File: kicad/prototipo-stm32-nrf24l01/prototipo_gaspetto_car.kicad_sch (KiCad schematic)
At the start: 11 parts, among them J1 Conn_01x07_Pin - TEST POINT, M1 Motor_DC, M2 Motor_DC, Q1 BC548, U1 YAAJ_BluePill_Part_Like_SWD_B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, U2 nRF24L01+, U3 L9110-M2, U4 L9110-M1, U5 5 to 3.3v

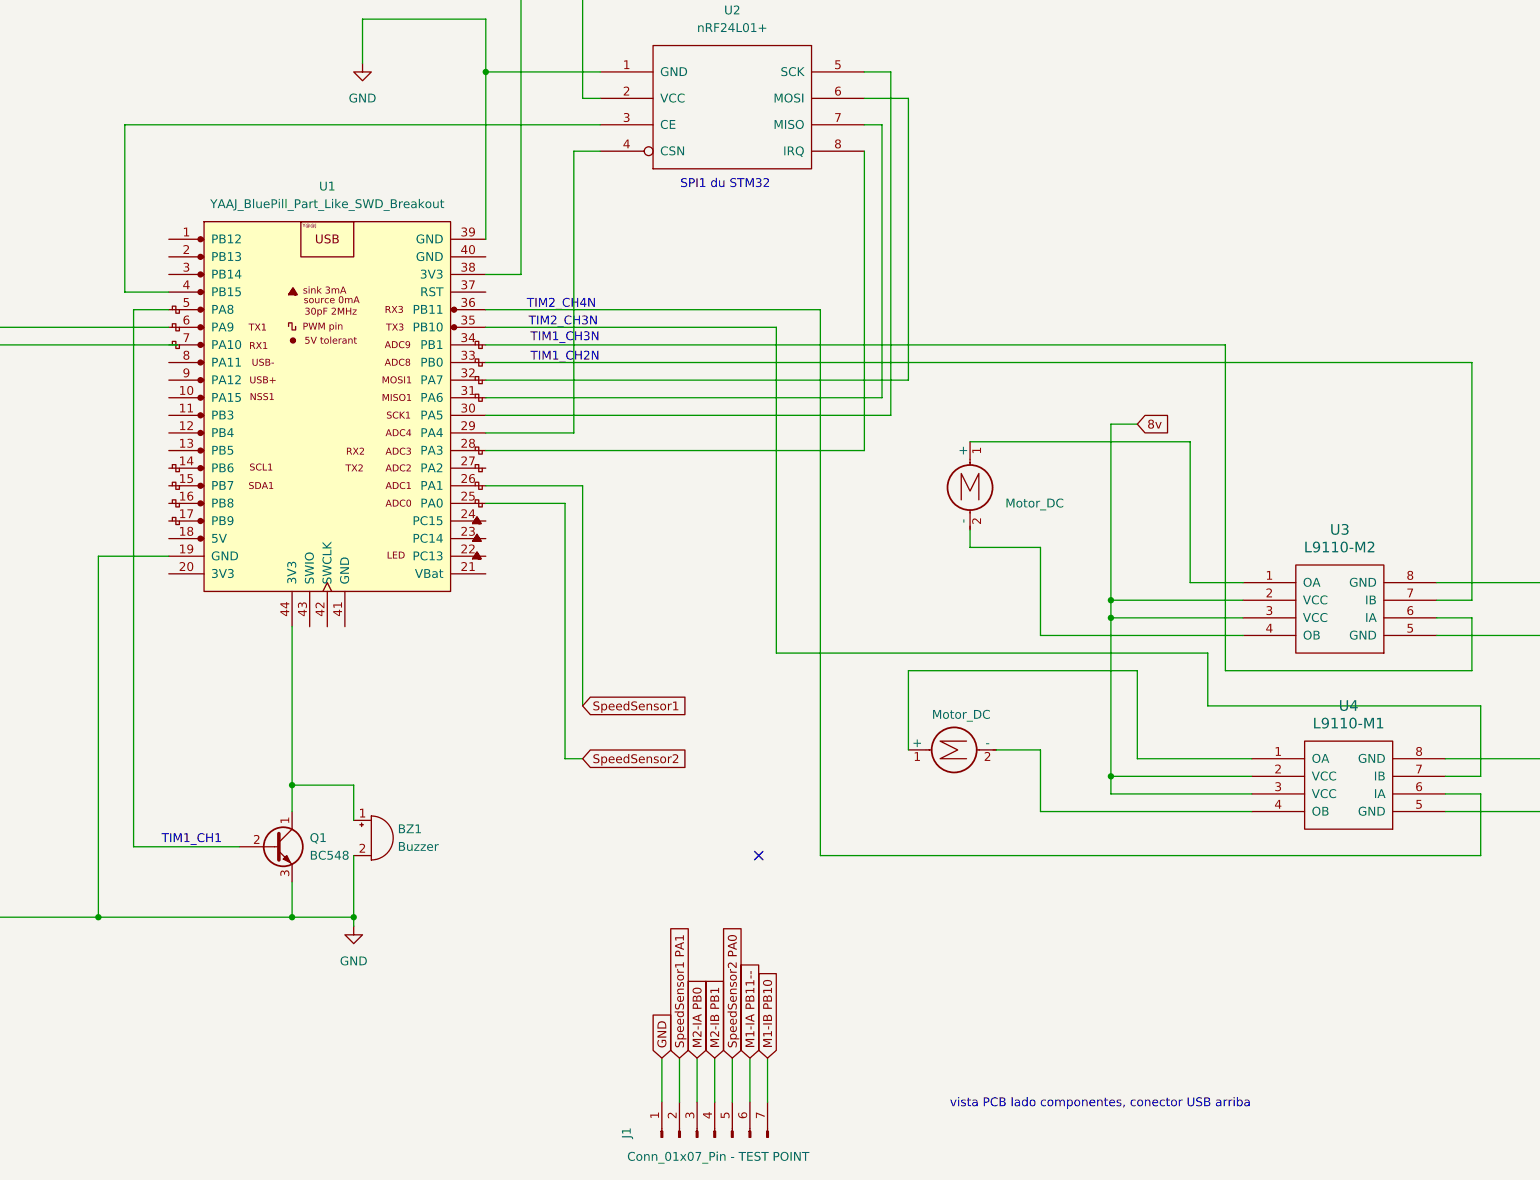
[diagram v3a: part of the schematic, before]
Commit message: car: motor and radio
- We receive radio commands and execute them. I have some issues
  controlling DC motors, will try to restructure a bit and add
  a PID controller.
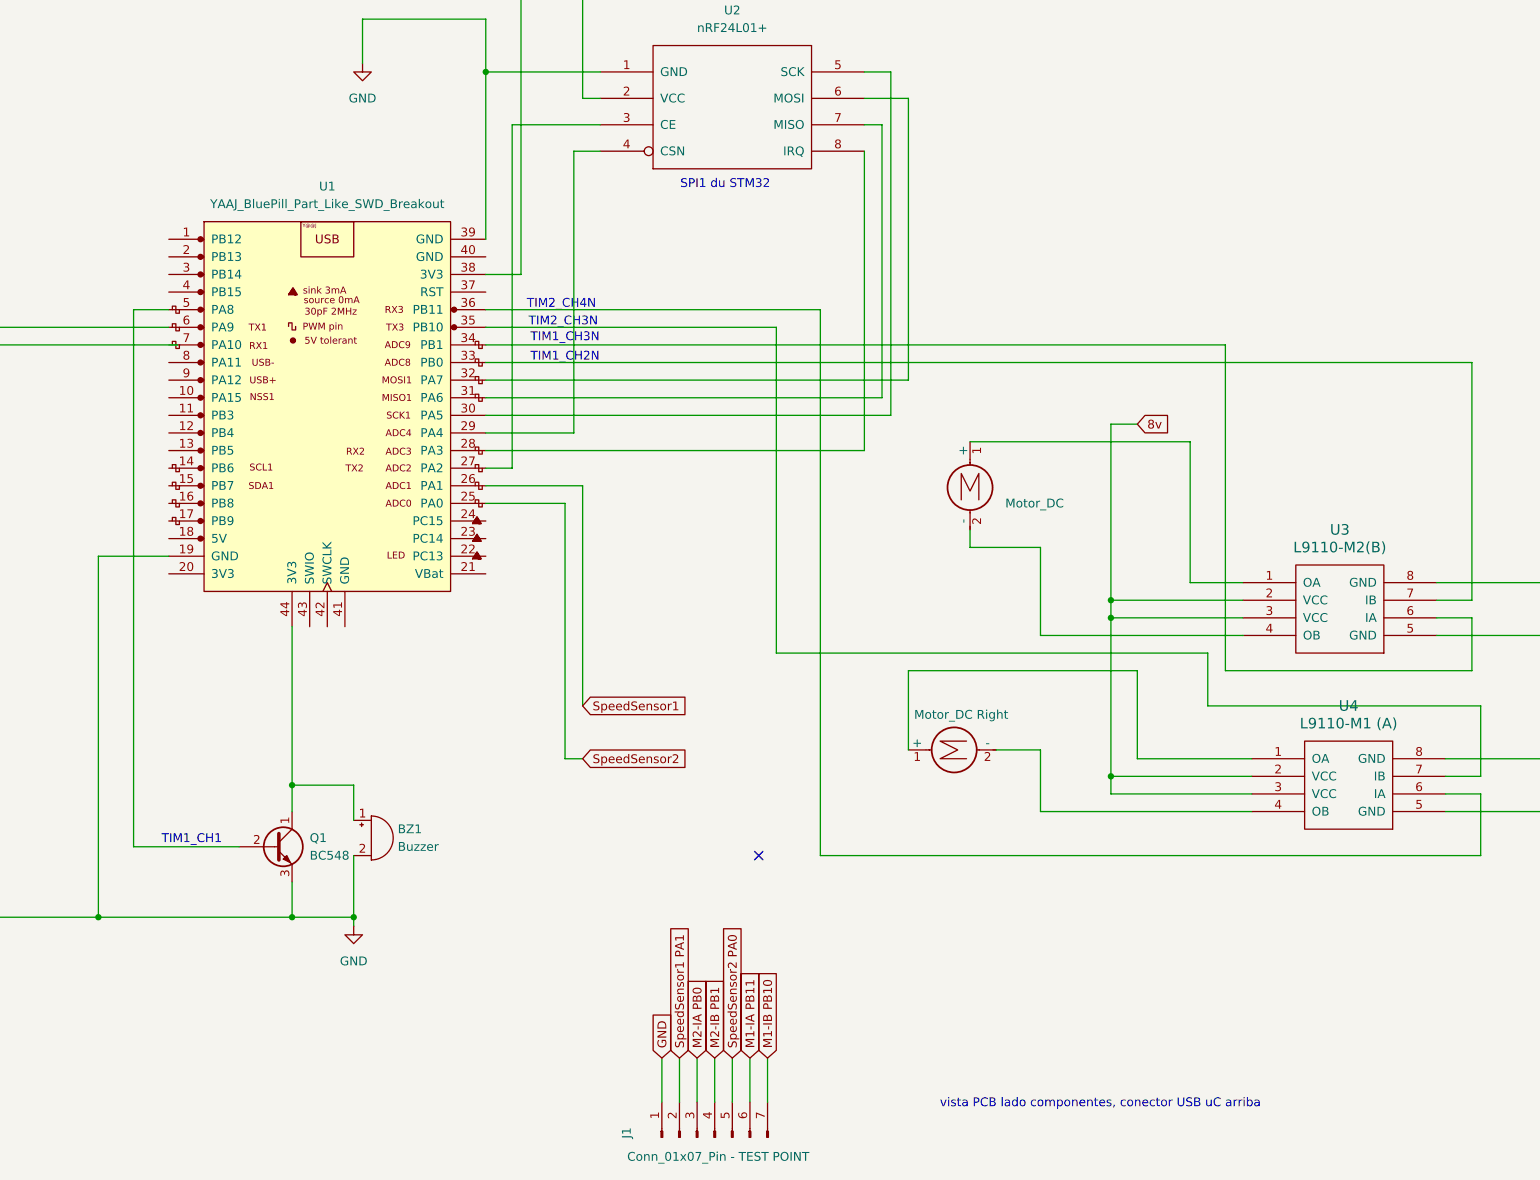
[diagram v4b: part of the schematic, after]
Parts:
- M1: value Motor_DC -> Motor_DC Right
- U3: value L9110-M2 -> L9110-M2(B)
- U4: value L9110-M1 -> L9110-M1 (A)
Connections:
- net at U1.27 (PA2): now also U2.3 (CE)
- net at U1.4 (PB15): no longer U2.3 (CE)
- net M1-IA PB11-- renamed M1-IA PB11
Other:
- note added: "vista PCB lado componentes, conector USB uC arriba"
- note removed: "vista PCB lado componentes, conector USB arriba"
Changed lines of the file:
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@@
 		)
 	)
-	(text "vista PCB lado componentes, conector USB arriba\n"
+	(text "vista PCB lado componentes, conector USB uC arriba\n"
 		(exclude_from_sim no)
 		(at 286.766 226.314 0)
@@
 	(wire
 		(pts
-			(xy 146.05 109.22) (xy 152.4 109.22)
-		)
-		(stroke
-			(width 0)
-			(type default)
-		)
-	)
-	(wire
-		(pts
 			(xy 170.18 157.48) (xy 170.18 180.34)
 		)
@@
 	(wire
 		(pts
+			(xy 201.93 134.62) (xy 201.93 85.09)
+		)
+		(stroke
+			(width 0)
+			(type default)
+		)
+	)
+	(wire
+		(pts
 			(xy 114.3 50.8) (xy 203.2 50.8)
 		)
@@
 	(wire
 		(pts
-			(xy 214.63 85.09) (xy 146.05 85.09)
+			(xy 214.63 85.09) (xy 201.93 85.09)
 		)
 		(stroke
@@
 	(wire
 		(pts
+			(xy 198.12 134.62) (xy 201.93 134.62)
+		)
+		(stroke
+			(width 0)
+			(type default)
+		)
+	)
+	(wire
+		(pts
 			(xy 341.63 168.91) (xy 302.26 168.91)
 		)
@@
 		(pts
 			(xy 354.33 184.15) (xy 336.55 184.15)
-		)
-		(stroke
-			(width 0)
-			(type default)
-		)
-	)
-	(wire
-		(pts
-			(xy 146.05 85.09) (xy 146.05 109.22)
 		)
 		(stroke
@@
 		)
 	)
-	(global_label "M1-IA PB11--"
+	(global_label "M1-IA PB11"
 		(shape input)
 		(at 236.22 219.71 90)
@@
 		)
 		(property "Intersheetrefs" "${INTERSHEET_REFS}"
-			(at 236.22 201.7267 90)
+			(at 236.22 204.8715 90)
 			(effects
 				(font
@@
 			)
 		)
-		(property "Value" "L9110-M2"
+		(property "Value" "L9110-M2(B)"
 			(at 321.31 146.05 0)
 			(effects
@@
 		(on_board yes)
 		(dnp no)
-		(fields_autoplaced yes)
 		(property "Reference" "M1"
 			(at 266.7 167.64 90)
@@
 			)
 		)
-		(property "Value" "Motor_DC"
+		(property "Value" "Motor_DC Right"
 			(at 266.7 170.18 90)
 			(effects
@@
 			)
 		)
-		(property "Value" "L9110-M1"
+		(property "Value" "L9110-M1 (A)"
 			(at 322.58 171.45 0)
 			(effects

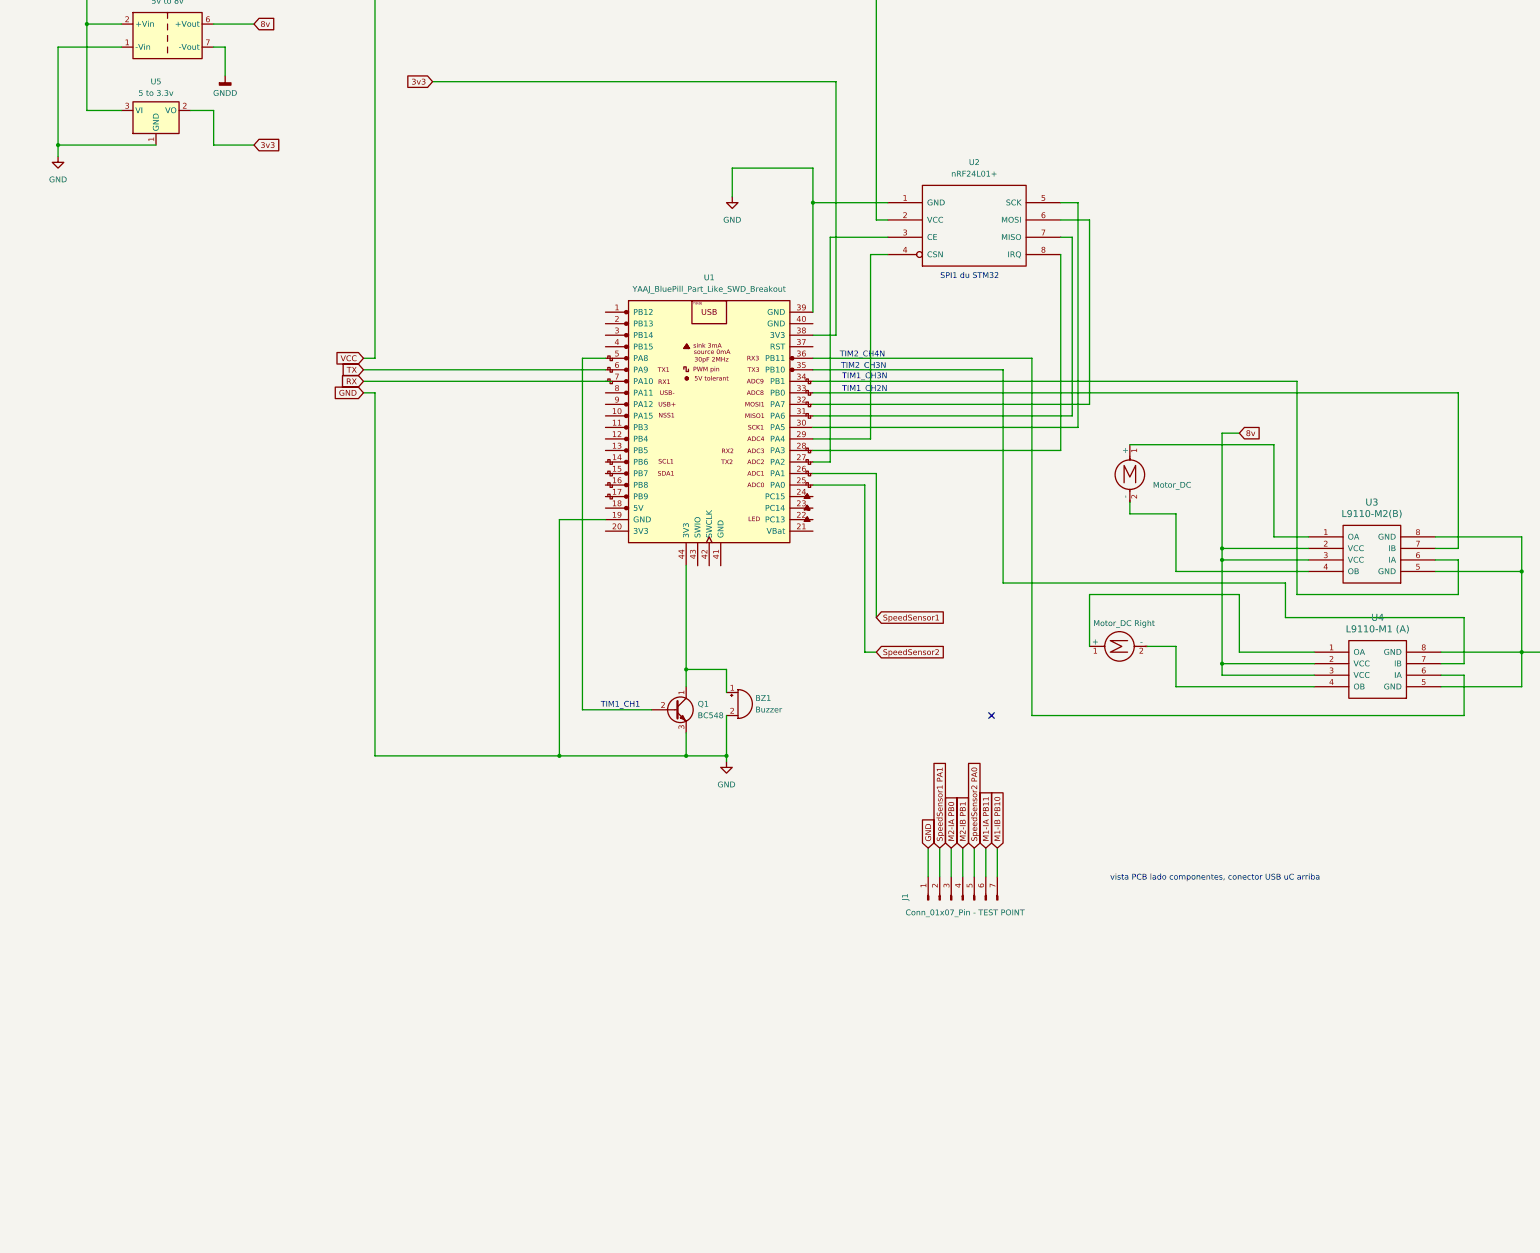
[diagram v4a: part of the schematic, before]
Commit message: car: schematic add mpu 6050
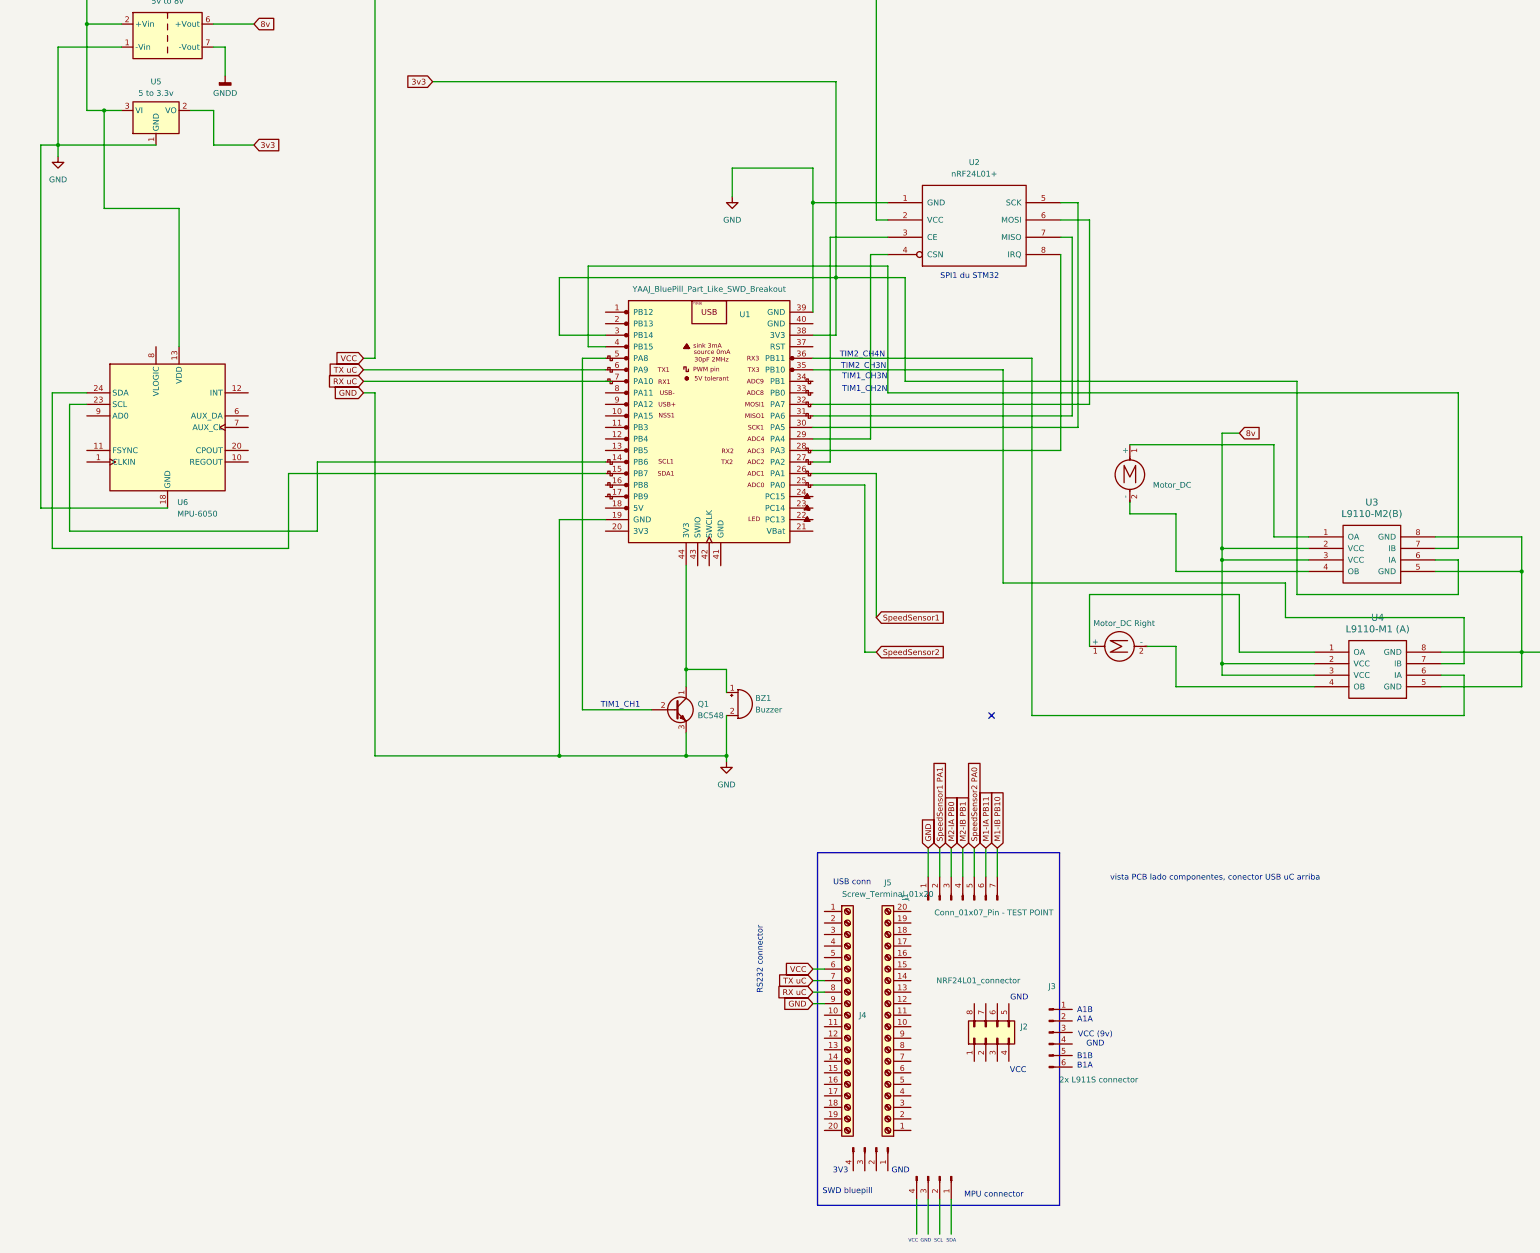
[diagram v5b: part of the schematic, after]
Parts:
- added J2: NRF24L01_connector, symbol Connector_Generic:Conn_02x04_Counter_Clockwise
- added J3: 2x L911S connector, symbol Connector:Conn_01x06_Pin
- added J4, J5: Screw_Terminal_01x20, symbol Connector:Screw_Terminal_01x20
- added J6: Conn_01x04_Pin, symbol Connector:Conn_01x04_Pin
- added MPU-6050: ~, symbol Connector:Conn_01x04_Pin
- added U6: MPU-6050, Sensor_Motion:InvenSense_QFN-24_4x4mm_P0.5mm, symbol Sensor_Motion:MPU-6050
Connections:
- net 3v3: now also U1.3 (PB14), U3.6 (IA)
- net 5v: now also J4.6 (Pin_6), U6.13 (VDD)
- net GND: now also J4.9 (Pin_9), U6.18 (GND)
- net at U1.14 (PB6): now also U6.23 (SCL)
- net at U1.15 (PB7): now also U6.24 (SDA)
- net at U1.33 (PB0): no longer U3.7 (IB)
- net at U1.34 (PB1): no longer U3.6 (IA)
- net at U1.4 (PB15): now also U3.7 (IB)
- net TX renamed TX uC
- net TX uC: now also J4.7 (Pin_7)
- new net RX uC: J4.8 (Pin_8)
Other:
- note added: "3V3"
- note added: "A1B A1A"
- note added: "B1B B1A"
- note added: "GND"
- note added: "MPU connector"
- note added: "RS232 connector"
- note added: "SCL"
- note added: "SDA"
- note added: "SWD bluepill"
- note added: "USB conn"
- note added: "VCC"
- note added: "VCC (9v) GND"
